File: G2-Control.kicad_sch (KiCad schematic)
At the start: 94 parts, among them J1 Conn_01x06_Pin, J102 Conn_01x06_Pin, J103 Conn_01x06_Pin, J104 Board Interconnect, J2 Q2_link, J3 Conn_01x07_Pin, J4 Conn_01x05_Pin, K1 SMI-12VDC-SL-2C, K2 SMI-12VDC-SL-2C, K3 SMI-12VDC-SL-2C, Q1 TIP122, Q2 2SK3566, Q3 2N5061, Q4 2N4403, Q5 BC847, Q6 IRF9530N, U1 LM317L_SOT-89, U2 748, U3 4N36, U4 78L05, U5 LMC555CMX

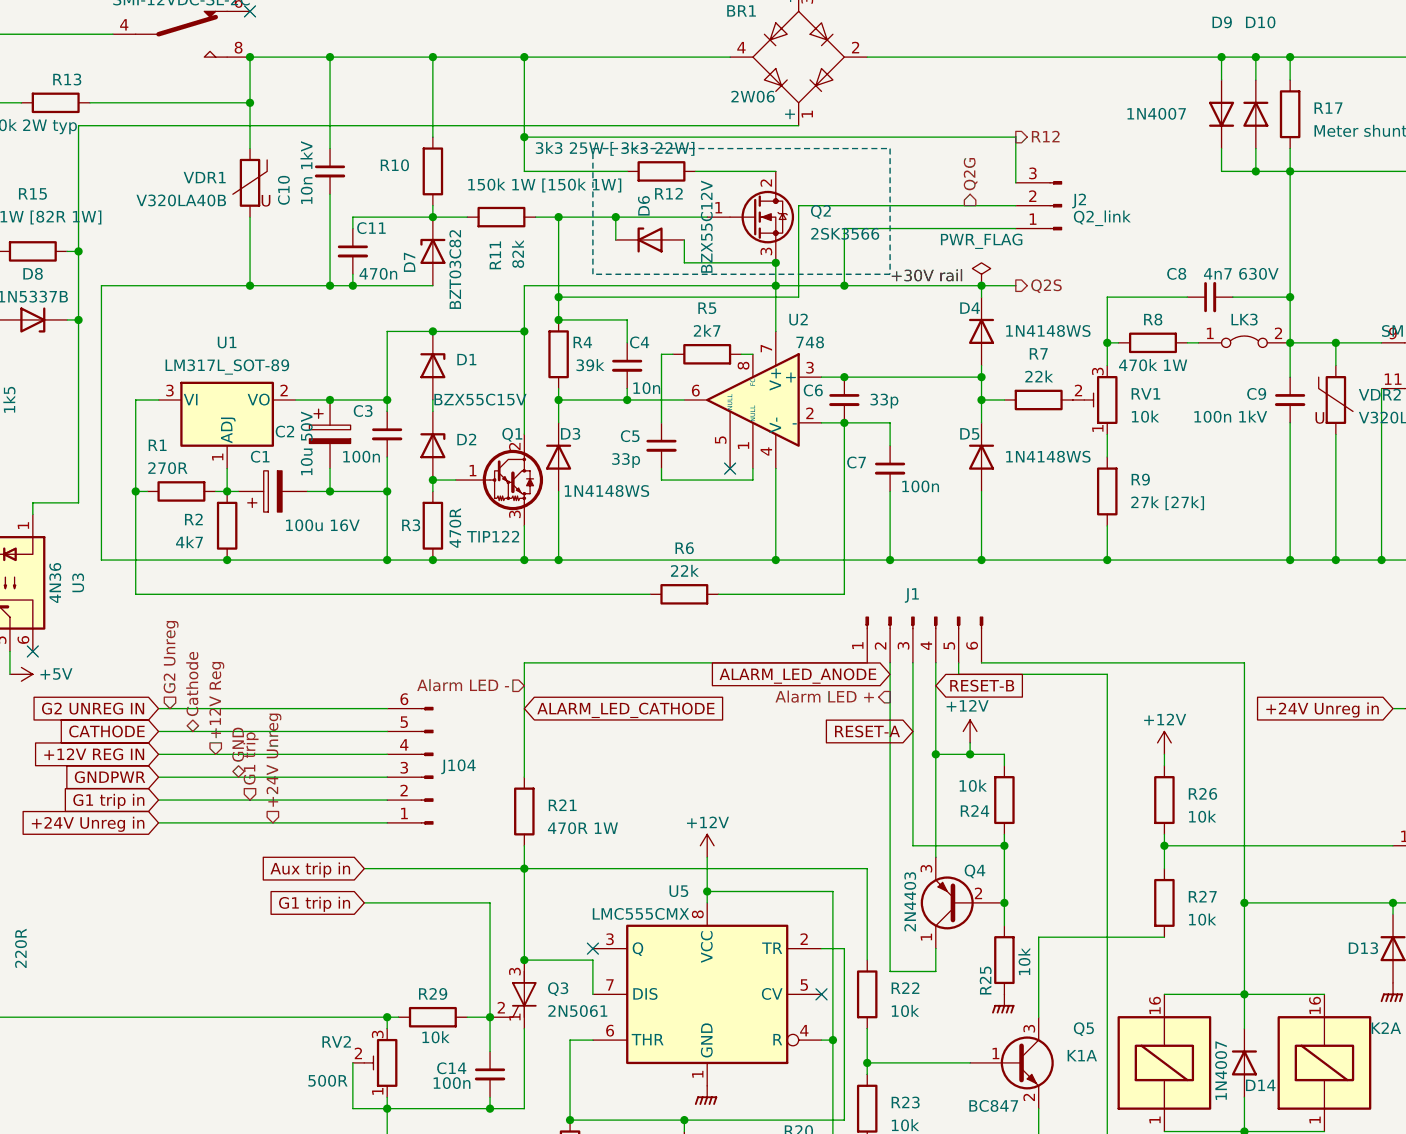
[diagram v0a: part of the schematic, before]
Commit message: Fixes for issues #7 #6 #3 #5
Connected U1 correctly.
Added D6 to the board
Added version number to silkscreen text.
Added high voltage warning
Turned Q1 around and moved it closer to the edge.
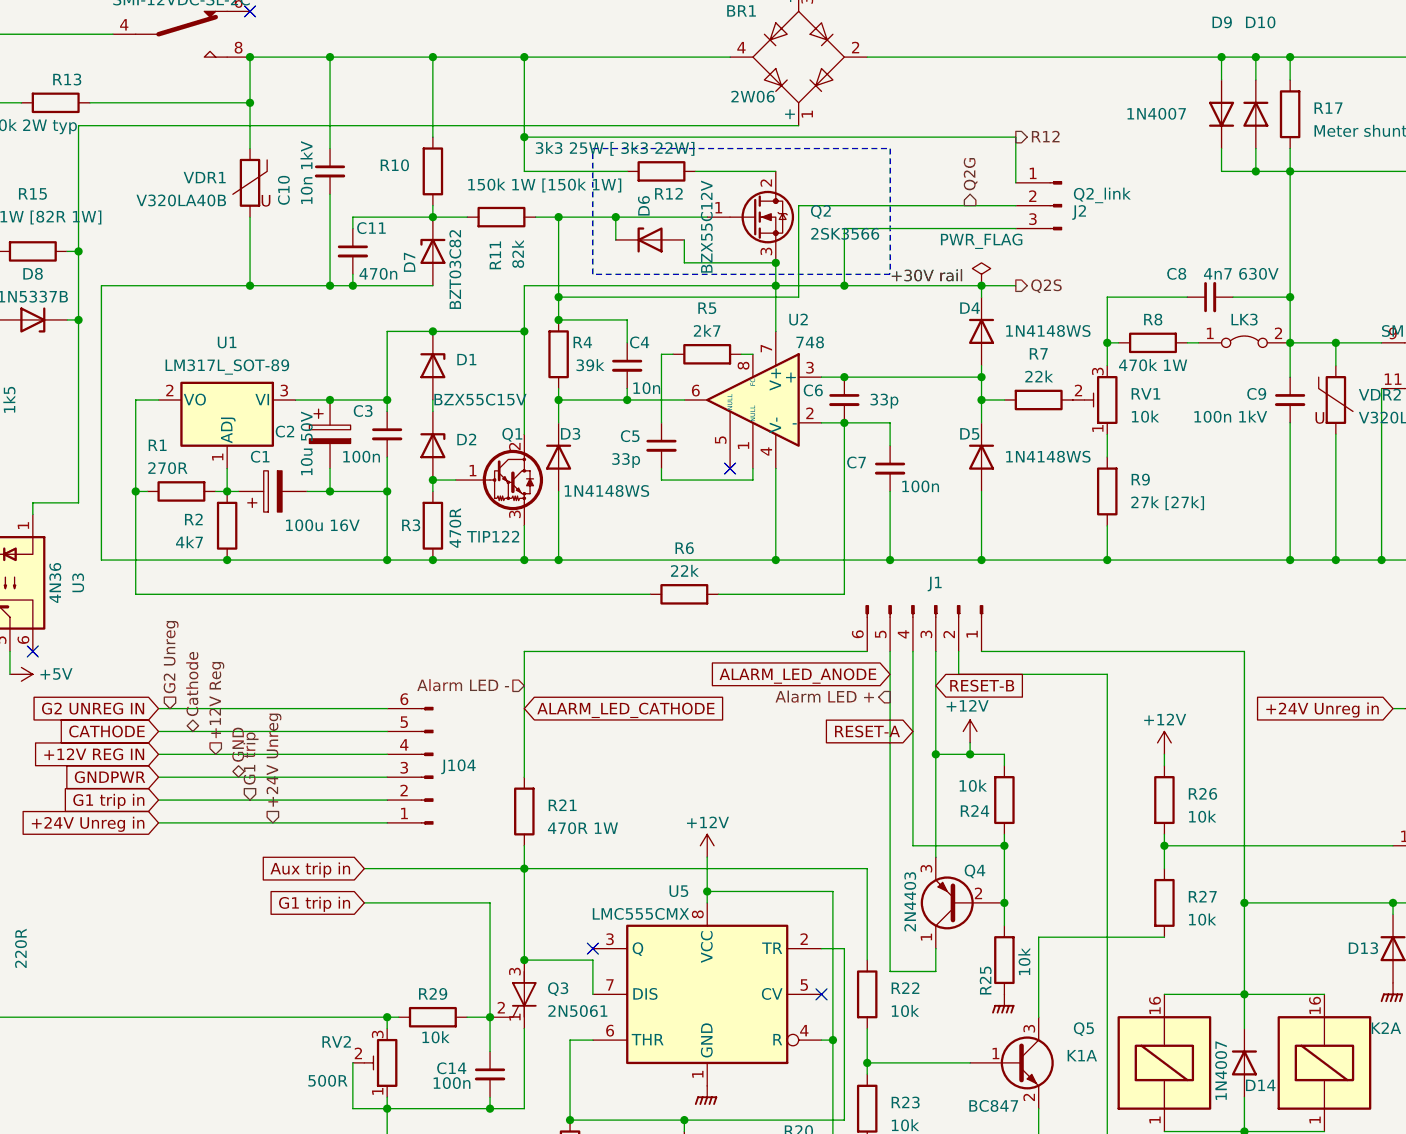
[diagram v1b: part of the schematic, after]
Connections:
- net +12V: now also J1.3 (Pin_3); no longer J1.4 (Pin_4)
- net +12/24V HV ENABLE: now also J1.1 (Pin_1); no longer J1.6 (Pin_6)
- net ALARM_LED_ANODE: now also J1.5 (Pin_5); no longer J1.2 (Pin_2)
- net ALARM_LED_CATHODE: now also J1.6 (Pin_6); no longer J1.1 (Pin_1)
- net PTT_L: now also J1.2 (Pin_2); no longer J1.5 (Pin_5)
- net Q2S: now also J2.3 (Pin_3), U1.3 (VI); no longer J2.1 (Pin_1), U1.2 (VO)
- net R12: now also J2.1 (Pin_1); no longer J2.3 (Pin_3)
- net RESET-A: now also J1.4 (Pin_4); no longer J1.3 (Pin_3)
- net at R1.1, R6.1: now also U1.2 (VO); no longer U1.3 (VI)
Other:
- company: (none) -> SM6FBQ
- title: (none) -> G2-Control Board
- moved on the sheet: J1, J2
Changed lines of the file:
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@@
 	(generator_version "8.0")
 	(paper "A4")
+	(title_block
+		(title "G2-Control Board")
+		(date "2024-04-05")
+		(rev "1.1.0")
+		(company "SM6FBQ")
+	)
 	(junction
 		(at 124.46 52.07)
@@
 	(wire
 		(pts
-			(xy 191.77 95.25) (xy 191.77 93.98)
+			(xy 191.77 95.25) (xy 191.77 92.71)
 		)
 		(stroke
@@
 	(wire
 		(pts
-			(xy 194.31 93.98) (xy 223.52 93.98)
+			(xy 194.31 92.71) (xy 223.52 92.71)
 		)
 		(stroke
@@
 	(wire
 		(pts
-			(xy 186.69 93.98) (xy 186.69 114.3)
+			(xy 186.69 92.71) (xy 186.69 114.3)
 		)
 		(stroke
@@
 	(wire
 		(pts
-			(xy 143.51 93.98) (xy 143.51 106.68)
+			(xy 143.51 92.71) (xy 143.51 106.68)
 		)
 		(stroke
@@
 	(wire
 		(pts
-			(xy 189.23 93.98) (xy 189.23 104.14)
+			(xy 189.23 92.71) (xy 189.23 104.14)
 		)
 		(stroke
@@
 	(wire
 		(pts
-			(xy 181.61 93.98) (xy 143.51 93.98)
-		)
-		(stroke
-			(width 0)
-			(type default)
-		)
-	)
-	(wire
-		(pts
 			(xy 196.85 114.3) (xy 196.85 120.65)
 		)
@@
 	(wire
 		(pts
+			(xy 143.51 92.71) (xy 181.61 92.71)
+		)
+		(stroke
+			(width 0)
+			(type default)
+		)
+	)
+	(wire
+		(pts
 			(xy 224.79 36.83) (xy 224.79 39.37)
 		)
@@
 	(wire
 		(pts
-			(xy 184.15 93.98) (xy 184.15 128.27)
+			(xy 184.15 92.71) (xy 184.15 128.27)
 		)
 		(stroke
@@
 	(wire
 		(pts
-			(xy 223.52 93.98) (xy 223.52 120.65)
+			(xy 223.52 92.71) (xy 223.52 120.65)
 		)
 		(stroke
@@
 		(lib_id "Regulator_Linear:LM317L_SOT-89")
 		(at 110.49 64.77 0)
+		(mirror y)
 		(unit 1)
 		(exclude_from_sim no)
@@
 	(symbol
 		(lib_id "Connector:Conn_01x03_Pin")
-		(at 203.2 43.18 180)
+		(at 203.2 43.18 0)
+		(mirror y)
 		(unit 1)
 		(exclude_from_sim no)
@@
 		(dnp no)
 		(property "Reference" "J2"
-			(at 204.47 42.545 0)
+			(at 204.47 43.815 0)
 			(do_not_autoplace yes)
 			(effects
@@
 		)
 		(property "Value" "Q2_link"
-			(at 204.47 44.45 0)
+			(at 204.47 41.91 0)
 			(effects
 				(font
@@
 		(exclude_from_sim no)
 		(in_bom yes)
-		(on_board no)
+		(on_board yes)
 		(dnp no)
 		(property "Reference" "D6"
@@
 	(symbol
 		(lib_id "Connector:Conn_01x06_Pin")
-		(at 186.69 88.9 90)
-		(mirror x)
+		(at 189.23 87.63 270)
 		(unit 1)
 		(exclude_from_sim no)
@@
 		(dnp no)
 		(property "Reference" "J1"
-			(at 186.69 86.36 90)
+			(at 189.23 85.09 90)
 			(effects
 				(font
@@
 		)
 		(property "Value" "Conn_01x06_Pin"
-			(at 187.96 87.63 90)
+			(at 187.96 86.36 90)
 			(effects
 				(font
@@
 		)
 		(property "Footprint" "Connector_Phoenix_MSTB:PhoenixContact_MSTBVA_2,5_6-G-5,08_1x06_P5.08mm_Vertical"
-			(at 186.69 88.9 0)
+			(at 189.23 87.63 0)
 			(effects
 				(font
@@
 		)
 		(property "Datasheet" "~"
-			(at 186.69 88.9 0)
+			(at 189.23 87.63 0)
 			(effects
 				(font
@@
 		)
 		(property "Description" ""
-			(at 186.69 88.9 0)
+			(at 189.23 87.63 0)
 			(effects
 				(font
@@
 		)
 		(property "Supplier" "Electrokit"
-			(at 186.69 88.9 0)
+			(at 189.23 87.63 0)
 			(effects
 				(font
@@
 		)
 		(property "Order #" "41017488"
-			(at 186.69 88.9 0)
+			(at 189.23 87.63 0)
 			(effects
 				(font

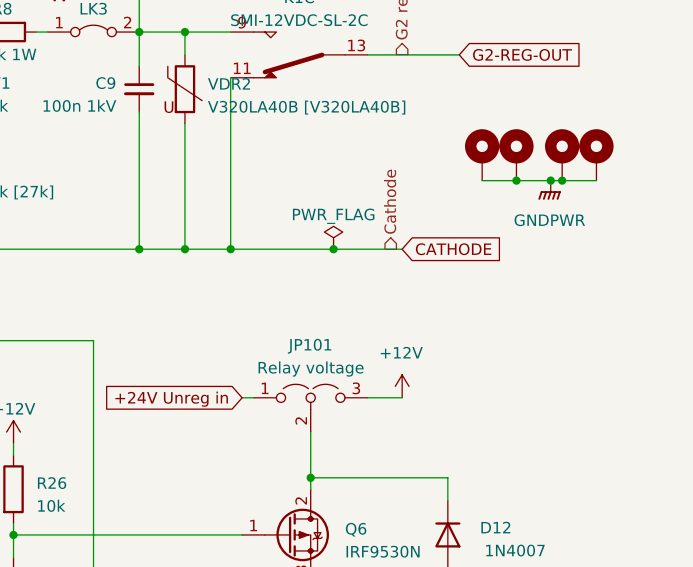
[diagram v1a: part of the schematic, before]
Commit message: Add new wiring and mounting hole to G2-Control schematic
Introduced a mounting hole to the G2-Control KiCad. The hole is
to be used as a low impedance connection between the CATHODE rail and chassis ground, in case of a cathode grounded PA.
Otherwise the connection should be connected to the high tension negative pole.
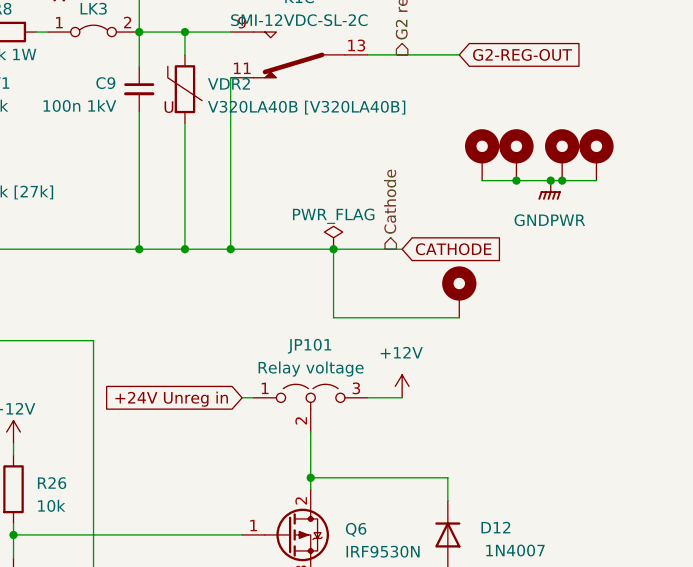
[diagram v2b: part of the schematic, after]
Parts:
- added H5: MountingHole_Pad, MountingHole:MountingHole_3.2mm_M3_DIN965_Pad, symbol Mechanical:MountingHole_Pad
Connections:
- net CATHODE: now also H5.1
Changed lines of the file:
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@@
 	(wire
 		(pts
+			(xy 264.16 90.17) (xy 250.19 90.17)
+		)
+		(stroke
+			(width 0)
+			(type default)
+		)
+	)
+	(wire
+		(pts
 			(xy 196.85 64.77) (xy 194.31 64.77)
 		)
@@
 	(wire
 		(pts
+			(xy 250.19 90.17) (xy 250.19 82.55)
+		)
+		(stroke
+			(width 0)
+			(type default)
+		)
+	)
+	(wire
+		(pts
 			(xy 266.7 74.93) (xy 270.51 74.93)
 		)
@@
 					(unit 1)
 				)
+			)
+		)
+	)
+	(symbol
+		(lib_id "Mechanical:MountingHole_Pad")
+		(at 264.16 87.63 0)
+		(unit 1)
+		(exclude_from_sim no)
+		(in_bom yes)
+		(on_board yes)
+		(dnp no)
+		(fields_autoplaced yes)
+		(property "Reference" "H5"
+			(at 267.335 85.725 0)
+			(effects
+				(font
+					(size 1.27 1.27)
+				)
+				(justify left)
+				(hide yes)
+			)
+		)
+		(property "Value" "MountingHole_Pad"
+			(at 267.335 88.265 0)
+			(effects
+				(font
+					(size 1.27 1.27)
+				)
+				(justify left)
+				(hide yes)
+			)
+		)
+		(property "Footprint" "MountingHole:MountingHole_3.2mm_M3_DIN965_Pad"
+			(at 264.16 87.63 0)
+			(effects
+				(font
+					(size 1.27 1.27)
+				)
+				(hide yes)
+			)
+		)
+		(property "Datasheet" ""
+			(at 264.16 87.63 0)
+			(effects
+				(font
+					(size 1.27 1.27)
+				)
+				(hide yes)
+			)
+		)
+		(property "Description" ""
+			(at 264.16 87.63 0)
+			(effects
+				(font
+					(size 1.27 1.27)
+				)
+				(hide yes)
+			)
+		)
+		(property "Supplier" "Elecrow"
+			(at 264.16 87.63 0)
+			(effects
+				(font
+					(size 1.27 1.27)
+				)
+				(hide yes)
+			)
+		)
+		(property "Order #" "----"
+			(at 264.16 87.63 0)
+			(effects
+				(font
+					(size 1.27 1.27)
+				)
+				(hide yes)
+			)
+		)
+		(pin "1"
+		)
+		(instances
+			(project "G2-Control"
+				(path "/712b5e85-571f-4504-95bc-7ff158b82674"
+					(reference "H5")
+					(unit 1)
+				)

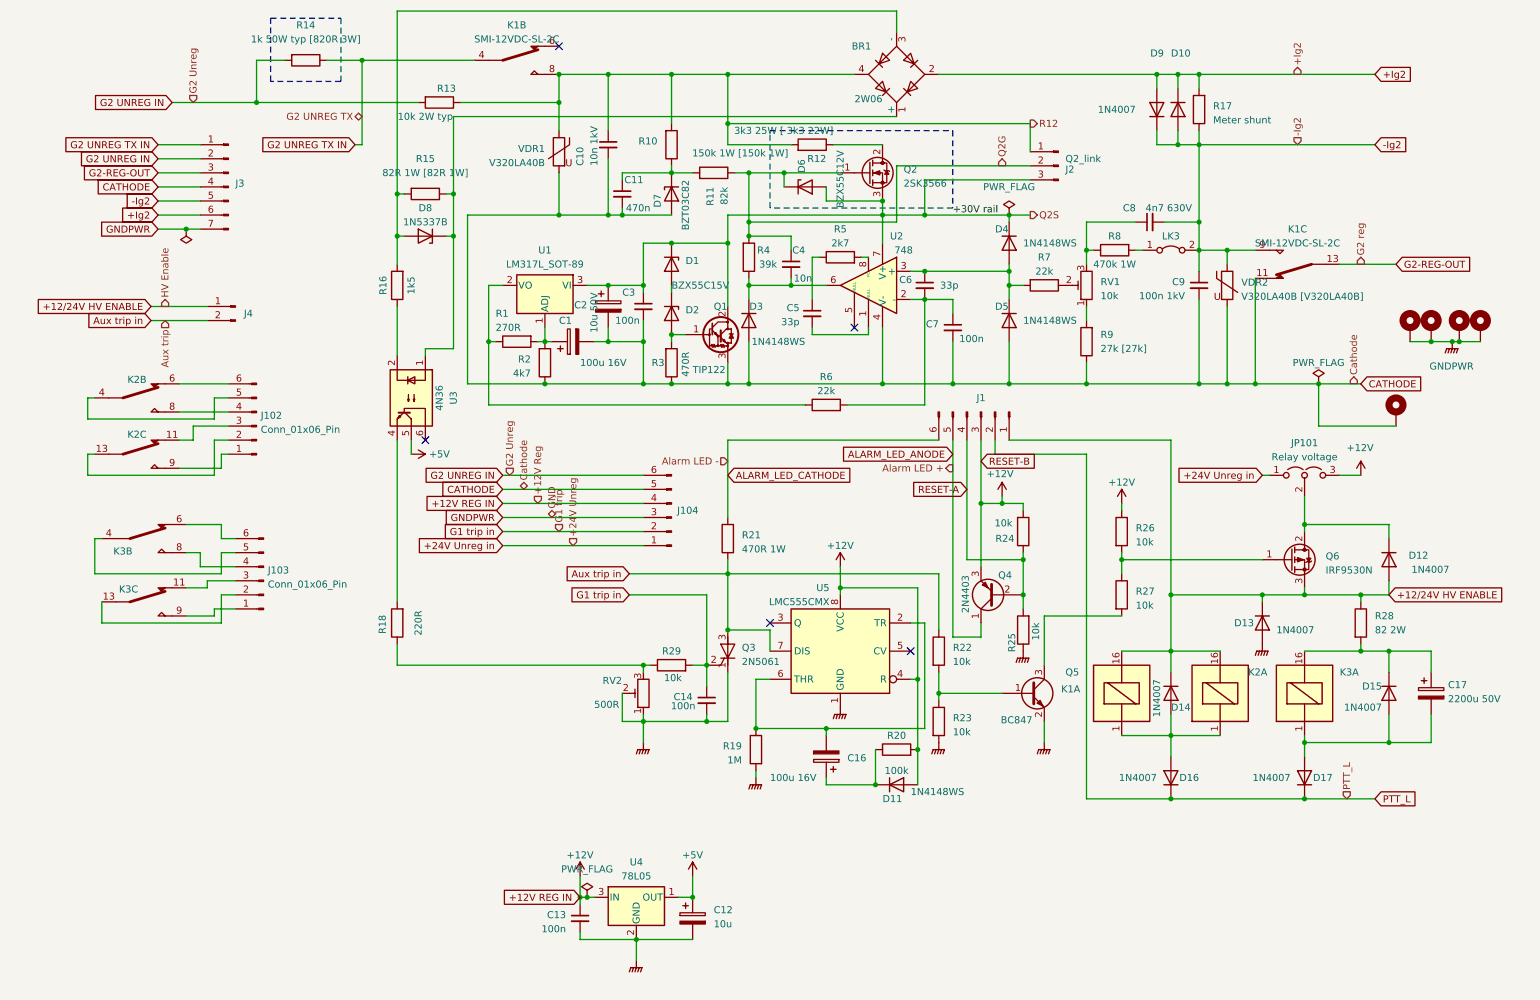
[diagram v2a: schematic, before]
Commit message: Cleaned up the G2-Control schematic.
Removed Netclass names from their flags and greyed the flags so thet they
interfere less with the actual schematic.

Moved things around to avoid collisions.
Moved D6 into the on-board space and shrunk the cutout for R12 and Q2
Moved BR1 to get less parallel wirings for the same signal.

Changed the SCR symbol in the library to make it more clear.
Shortened the gate pin of Q2 to free some vertical space.

Changed the values of some components that need to be configured to have an asterisk instead of a default value.
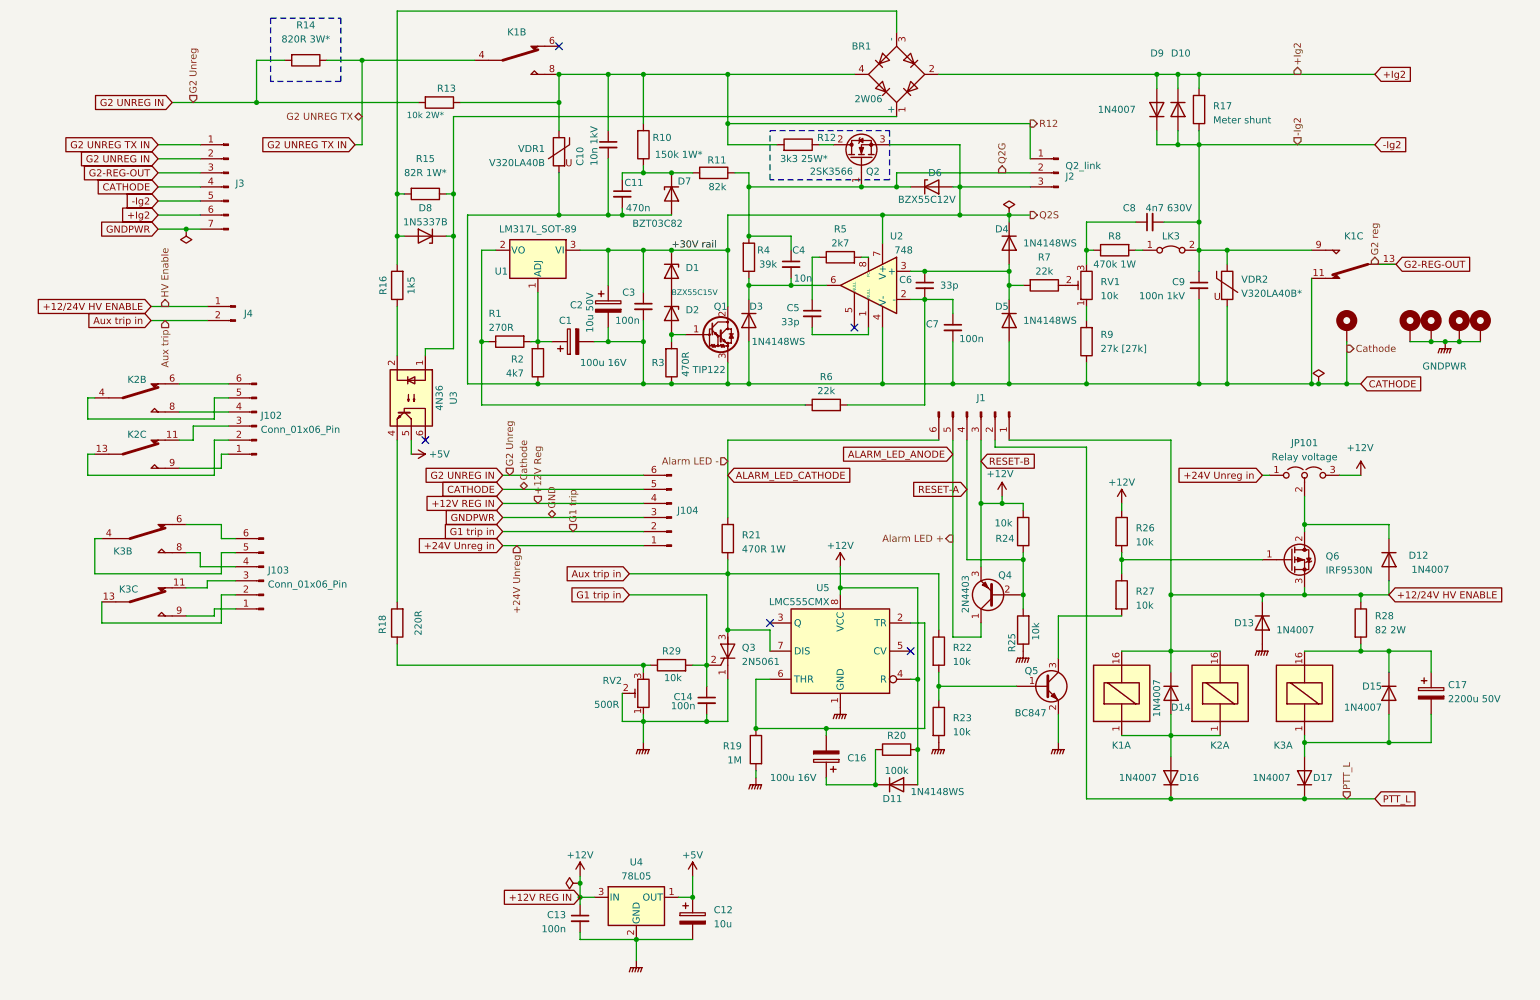
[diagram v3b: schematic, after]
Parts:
- R10: value 150k 1W [150k 1W] -> 150k 1W*
- R12: value 3k3 25W [ 3k3 22W] -> 3k3 25W*
- R13: value 10k 2W typ -> 10k 2W*
- R14: value 1k 50W typ [820R 3W] -> 820R 3W*
- R15: value 82R 1W [82R 1W] -> 82R 1W*
- VDR2: value V320LA40B [V320LA40B] -> V320LA40B*
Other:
- moved on the sheet: D1, D6, J2, K1C, Q2, Q3, Q5, R1, R10, R12, R2, U1
